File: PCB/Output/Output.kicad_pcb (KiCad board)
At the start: 2 copper layers, 47.7 x 34.3 mm, 46 parts, among them J1 USB-C, J10 O8, J11 O9, J12 O10, J13 Shelly, J2 POWER, J3 O1, J4 O2, J5 O3, J6 O4, J7 O5, J8 O6, J9 O7, U1 ESP32-PICO-MINI-02, U10 QR, U11 VEML6040, U12 LMR16006YDDCR, U2 FT231XQ, U3 ISL89410, U4 ISL89410, U5 ISL89410, U6 ISL89410, U7 ISL89410, U9 AA

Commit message: VCUT
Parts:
- removed U11: VEML6040, RevK:VEML6040
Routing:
- net SCL: track 7.19 -> 0.00 mm
- net SDA: track 3.32 -> 0.00 mm
- net +3.3V: track 101.1 -> 100.0 mm, vias 5 -> 4

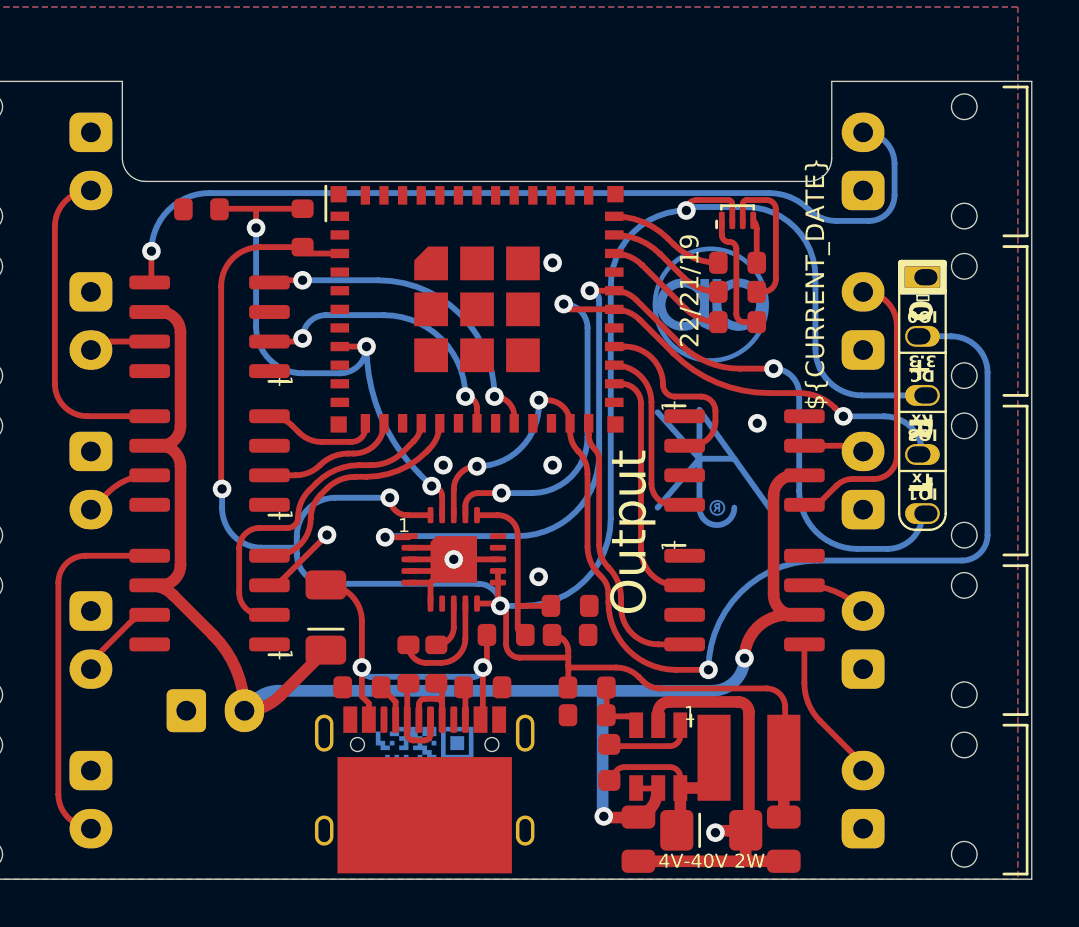
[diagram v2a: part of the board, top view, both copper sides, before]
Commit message: New reg, LED, UART
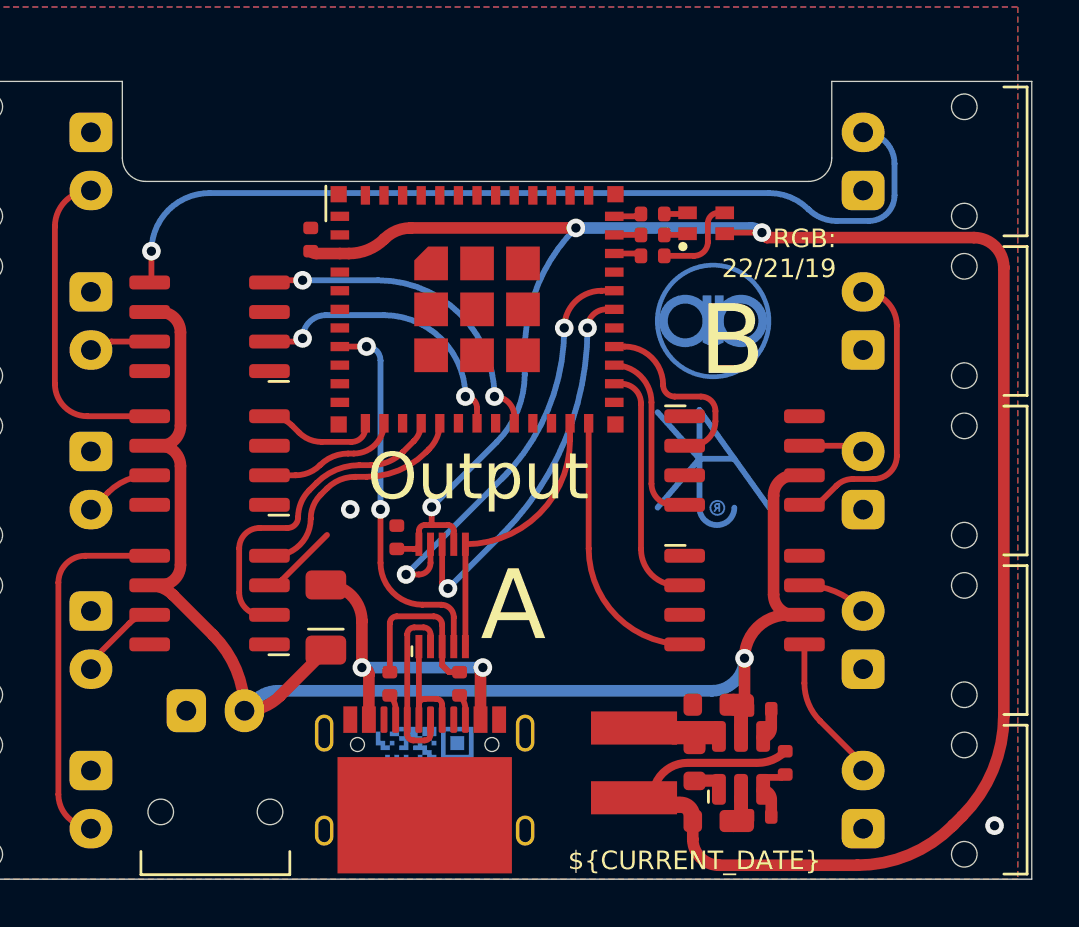
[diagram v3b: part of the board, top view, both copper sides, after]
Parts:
- removed C5: 1uF, RevK:C_0603
- removed C6: 100nF, RevK:C_0603_
- removed C7: 2.2uF, RevK:C_0805_
- removed C8: 10uF, RevK:C_0805_
- removed D1: LED_BARG, RevK:MHS190RGBCT
- removed D4: Schottky, RevK:D_1206_
- removed J13: Shelly, RevK:Shelly
- removed L2: 6.8uH, RevK:L_4x4_
- removed R1, R3: 10k, RevK:R_0603
- removed R10: 100R, RevK:R_0603
- removed R13: 100k 1%, RevK:R_0603
- removed R14: 30k 1%, RevK:R_0603
- removed R2: 4k7, RevK:R_0603
- removed R6, R7: 27R, RevK:R_0603
- removed R8: 300R, RevK:R_0603
- removed R9: 1K, RevK:R_0603
- removed U12: LMR16006YDDCR, RevK:SOT-23-Thin-6-Reg
- removed U2: FT231XQ, RevK:QFN-20-1EP_4x4mm_P0.5mm_EP2.5x2.5mm
- added C2: 0.1uF, RevK:C_0402, F.Cu at (101.3, 45.8)
- added C3: 10uF 50V, RevK:C_0603_, F.Cu at (114.8, 53.0)
- added C4: 10uF 6.3V, RevK:C_0603_, F.Cu at (114.8, 58.0)
- added C9: 100nF, RevK:C_0603_, F.Cu at (114.1, 55.5)
- added D3: RGB, RevK:LED-RGB-1.6x1.6, F.Cu at (114.6, 32.3)
- added L1: 10uH, RevK:L_4x4_, F.Cu at (111.5, 55.5)
- added R11: 680R, RevK:R_0402, F.Cu at (112.3, 32.8)
- added R12: 2K, RevK:R_0402, F.Cu at (112.3, 31.9)
- added R15: 220R, RevK:R_0402, F.Cu at (112.3, 33.7)
- added R16: 124k, RevK:R_0402_, F.Cu at (118.0, 55.5)
- added R17: 39k2, RevK:R_0402_, F.Cu at (116.9, 57.8)
- added R18: 1M, RevK:R_0402_, F.Cu at (116.9, 53.2)
- added U11: CH340X, RevK:CH340X, F.Cu at (103.2, 48.3)
- added U8: MD8942, RevK:SOT-23-6-MD8942, F.Cu at (116.1, 55.5)
- C1: footprint RevK:C_0603 -> RevK:C_0402
- J2: footprint RevK:Molex_MiniSPOX_H2RA -> RevK:PTSM-HH1-2-RA
- R4, R5: footprint RevK:R_0603 -> RevK:R_0402
- moved C1 20.3 mm to (97.6, 33.0), turned to 90 degrees
- moved R4 1.21 mm to (101.0, 52.1), turned to 90 degrees
- moved R5 1.01 mm to (104.0, 52.1), turned to -90 degrees
- moved U9 0.71 mm to (114.9, 36.5)
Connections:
- J1 pad A6: Net-(J1-D+-PadA6) -> D+
- J1 pad A7: Net-(J1-D--PadA7) -> D-
- J1 pad B6: Net-(J1-D+-PadA6) -> D+
- J1 pad B7: Net-(J1-D--PadA7) -> D-
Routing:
- net BOOT: track 48.4 -> 12.0 mm, vias 3 -> 0
- net O: track 41.7 -> 18.5 mm, vias 3 -> 2
- net I: track 31.3 -> 16.7 mm, vias 3 -> 2
- net +3.3V: track 100.0 -> 88.8 mm, vias 4 -> 3
- net Net-(U2-CBUS3): track 8.10 -> 0.00 mm
- net EN: track 24.5 -> 16.4 mm, vias 3 -> 2
- net Net-(D1-RK): track 6.40 -> 0.00 mm
- net +12V: track 66.6 -> 60.8 mm, vias 2 -> 1
- net Net-(D1-BK): track 5.43 -> 0.00 mm
- net B: track 5.52 -> 1.18 mm
- net R: track 5.25 -> 1.15 mm
- net Net-(J1-D--PadA7): track 4.06 -> 0.00 mm
- net GND: track 14.5 -> 10.6 mm, vias 8 -> 2
- net G: track 5.02 -> 1.18 mm
- net Net-(D3-BK): track 0.00 -> 3.68 mm
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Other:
- board text added: "A"
- board text added: "B"
- board text added: "RGB: 22/21/19"
- board text added: "ss.revk.uk"
- board text removed: "22/21/19"

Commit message: Panel
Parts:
- added PCB1: 70x70, RevK:PCB7070, F.Cu at (100.0, 100.0)
- added V1: ~, RevK:VCUT70, F.Cu at (100.0, 83.2)
- added V2: ~, RevK:VCUT70, F.Cu at (100.0, 117.5)
- added V3: ~, RevK:VCUT70, B.Cu at (76.2, 100.0)
- added V4: ~, RevK:VCUT70, B.Cu at (123.9, 100.0)
- moved R12 57.2 mm to (107.6, 88.9)
- moved AJK1 57.2 mm to (109.6, 99.4)
- moved C1 57.2 mm to (92.9, 90.0)
- moved C2 57.2 mm to (96.6, 102.8)
- moved C3 57.2 mm to (110.1, 110.0)
- moved C4 57.2 mm to (110.1, 115.0)
- moved C9 57.2 mm to (109.4, 112.5)
- moved D2 57.2 mm to (93.5, 106.2)
- moved D3 57.2 mm to (109.9, 89.3)
- moved J10 57.2 mm to (116.7, 93.5)
- moved J11 57.2 mm to (116.7, 86.6)
- moved J12 57.2 mm to (83.5, 93.5)
- moved J3 57.2 mm to (83.5, 86.6)
- moved J4 57.2 mm to (83.5, 100.4)
- moved J5 57.2 mm to (83.5, 114.1)
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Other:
- board size 47.7 x 34.3 mm -> 70 x 70 mm

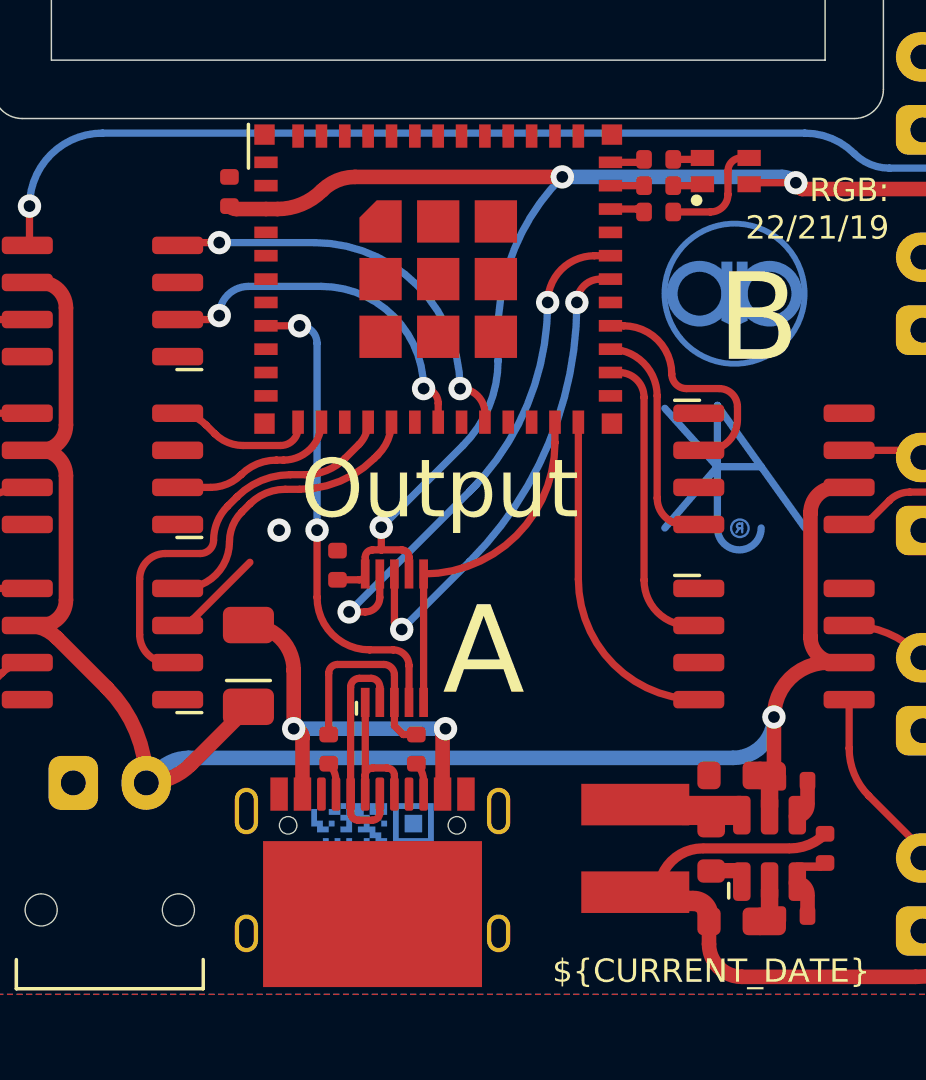
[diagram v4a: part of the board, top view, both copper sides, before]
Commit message: Fix output driver
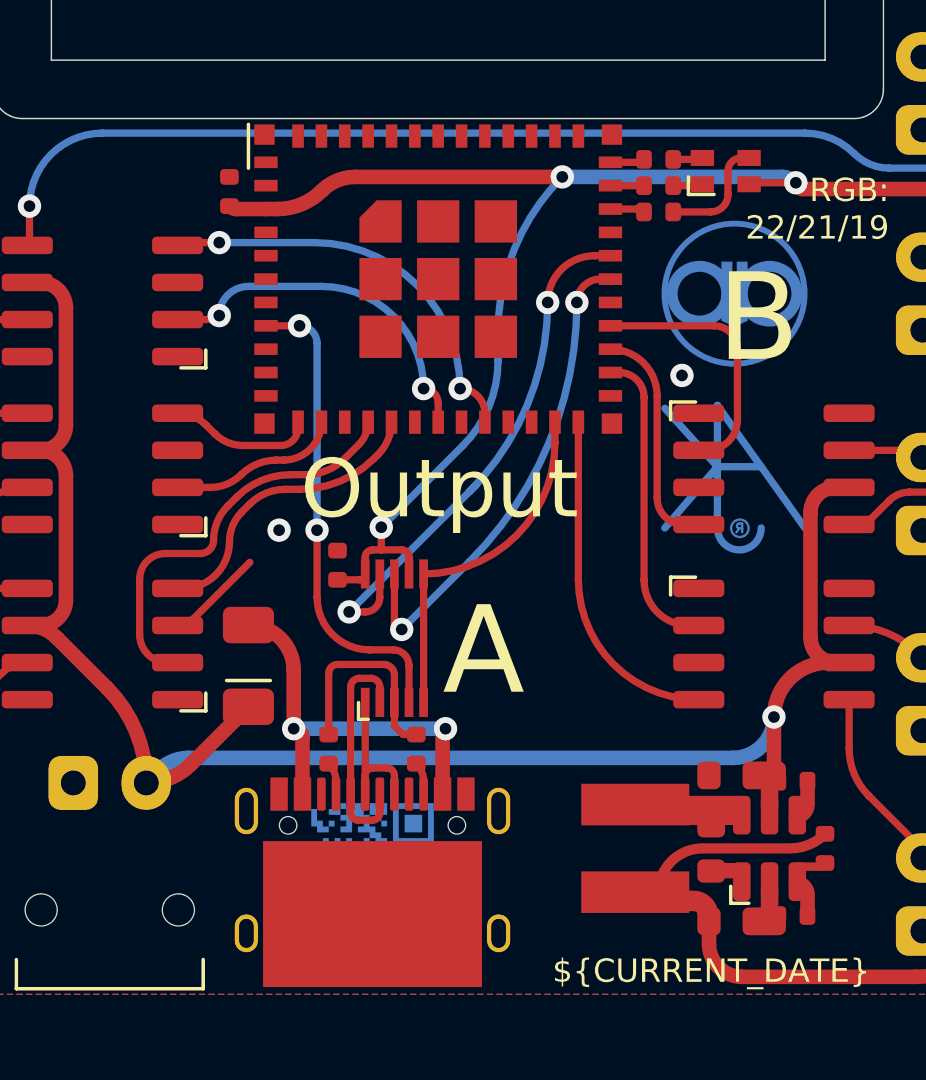
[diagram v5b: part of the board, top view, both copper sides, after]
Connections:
- U3 pad 1: unconnected-(U3-NC-Pad1) -> GND
- U3 pad 8: unconnected-(U3-NC-Pad8) -> GND
- U4 pad 1: unconnected-(U4-NC-Pad1) -> GND
- U4 pad 8: unconnected-(U4-NC-Pad8) -> GND
- U6 pad 1: unconnected-(U6-NC-Pad1) -> GND
- U6 pad 8: unconnected-(U6-NC-Pad8) -> GND
- U7 pad 1: unconnected-(U7-NC-Pad1) -> GND
- U7 pad 8: unconnected-(U7-NC-Pad8) -> GND
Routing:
- net OUT7: track 7.87 -> 8.80 mm
- net GND: vias 2 -> 3

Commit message: Driver
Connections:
- U3 pad 1: GND -> unconnected-(U3-~{EN}_A-Pad1)
- U3 pad 8: GND -> unconnected-(U3-~{EN}_B-Pad8)
- U4 pad 1: GND -> unconnected-(U4-~{EN}_A-Pad1)
- U4 pad 8: GND -> unconnected-(U4-~{EN}_B-Pad8)
- U6 pad 1: GND -> unconnected-(U6-~{EN}_A-Pad1)
- U6 pad 8: GND -> unconnected-(U6-~{EN}_B-Pad8)
- U7 pad 1: GND -> unconnected-(U7-~{EN}_A-Pad1)
- U7 pad 8: GND -> unconnected-(U7-~{EN}_B-Pad8)

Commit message: 3D
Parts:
- moved R17 1.21 mm to (113.3, 114.3), turned to -90 degrees
- moved R18 1.21 mm to (113.3, 110.7), turned to -90 degrees
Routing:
- net GND: track 10.6 -> 12.6 mm
